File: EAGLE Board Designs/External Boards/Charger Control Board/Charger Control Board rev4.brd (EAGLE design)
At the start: 80.5 x 83.1 mm, 81 parts

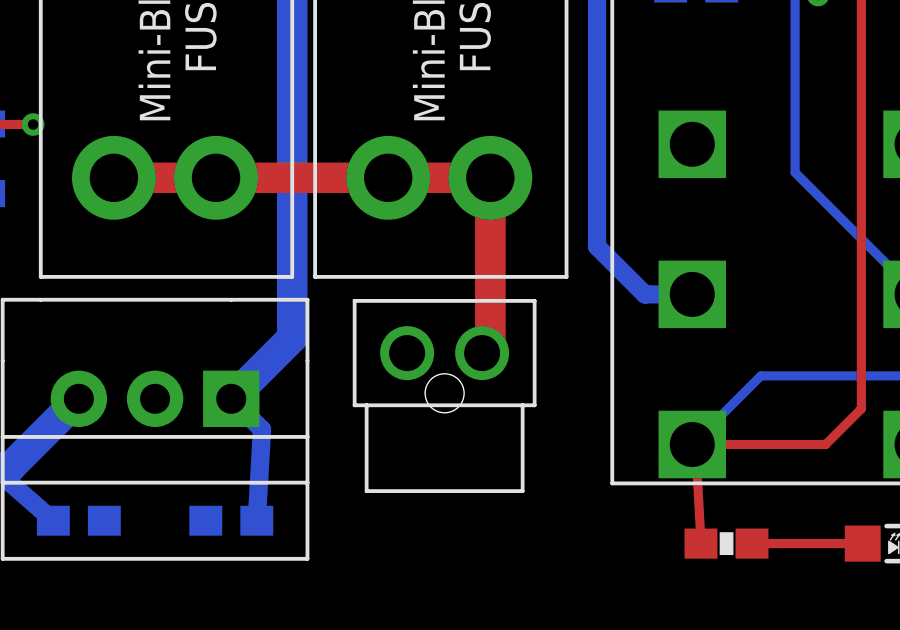
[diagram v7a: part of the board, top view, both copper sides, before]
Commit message: Added 0603 zener to protect 12V rail
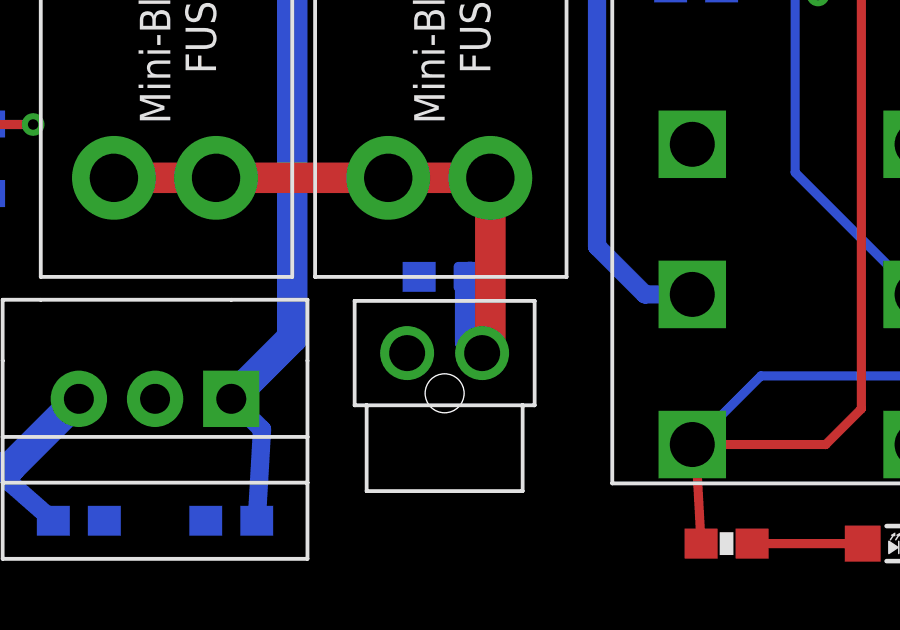
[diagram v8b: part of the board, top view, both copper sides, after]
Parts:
- added D2: DIODE_ZENER0603, HyTechDevices:0603_D
- ZENER: value (none) -> DIODE_ZENER
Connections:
- net +12VIN: now also D2.C
- net GND: now also D2.A
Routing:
- net +12VIN: track 18.5 -> 21.2 mm
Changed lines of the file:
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@@
 <attribute name="VALUE" x="-45.974" y="52.324" size="0.8128" layer="27" rot="R270" align="bottom-center"/>
 </element>
-<element name="ZENER" library="HyTechDevices" package="SOT23" value="" x="-71.12" y="37.846" smashed="yes" rot="MR0">
+<element name="ZENER" library="HyTechDevices" package="SOT23" value="DIODE_ZENER" x="-71.12" y="37.846" smashed="yes" rot="MR0">
 <attribute name="NAME" x="-71.12" y="38.1762" size="0.635" layer="52" font="vector" rot="MR0" align="top-center"/>
 <attribute name="VALUE" x="-72.517" y="38.735" size="0.3048" layer="28" rot="MR0" align="bottom-center"/>
@@
 <attribute name="NAME" x="-57.4421" y="52.324" size="0.3048" layer="26" rot="MR90" align="bottom-center"/>
 <attribute name="VALUE" x="-58.8772" y="52.324" size="0.3048" layer="28" rot="MR90" align="top-center"/>
+</element>
+<element name="D2" library="HyTechDevices" package="0603_D" value="DIODE_ZENER0603" x="-55.118" y="31.75" smashed="yes" rot="MR180">
+<attribute name="NAME" x="-55.118" y="31.115" size="0.4064" layer="26" rot="MR180" align="bottom-center"/>
+<attribute name="VALUE" x="-55.118" y="32.385" size="0.4064" layer="28" rot="MR180" align="top-center"/>
 </element>
 </elements>
@@
 <wire x1="-68.834" y1="36.83" x2="-70.154" y2="36.83" width="0.3048" layer="16"/>
 <wire x1="-70.154" y1="36.83" x2="-70.17" y2="36.846" width="0.3048" layer="16"/>
+<contactref element="D2" pad="A"/>
 </signal>
 <signal name="CANH">
@@
 <wire x1="-53.868" y1="29.21" x2="-53.594" y2="29.484" width="1.016" layer="1"/>
 <wire x1="-53.594" y1="29.484" x2="-53.594" y2="35.052" width="1.016" layer="1"/>
+<contactref element="D2" pad="C"/>
+<wire x1="-53.868" y1="29.21" x2="-54.268" y2="29.61" width="1.016" layer="16"/>
+<wire x1="-54.268" y1="29.61" x2="-54.268" y2="31.75" width="1.016" layer="16"/>
 </signal>
 <signal name="N$31">
